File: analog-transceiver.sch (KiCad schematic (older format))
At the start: 142 parts, among them J1 BNC, J2 AF In, J3 AF Out, Q1 2N3904, Q10 2N3904, Q11 2N3904, Q12 2N3904, Q13 2N3904, Q14 2N3904, Q15 2N3904, Q16 2N3904, Q17 2N3904, Q18 BF245A, Q19 2N3906, Q2 2N3904, Q20 2N3904, Q21 BF245A, Q25 BD139, Q26 BD140, Q3 BF245A, SW1 SW_DPDT_x2, SW2 SW_DPDT_x2, T1 2:8 Turns 43-material? iron p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, T2 iron powerder, Y1 10MHz, Y2 10MHz, Y3 10MHz, Y4 10MHz

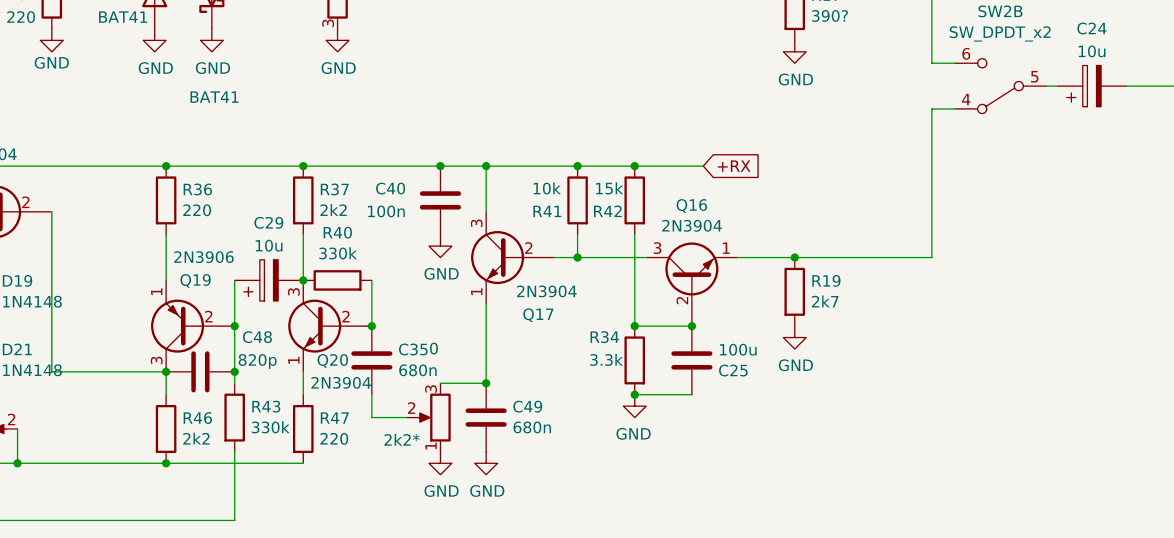
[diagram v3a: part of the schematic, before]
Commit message: Removed one stage from audio amplifier since the pre-amp should provide enough gain.
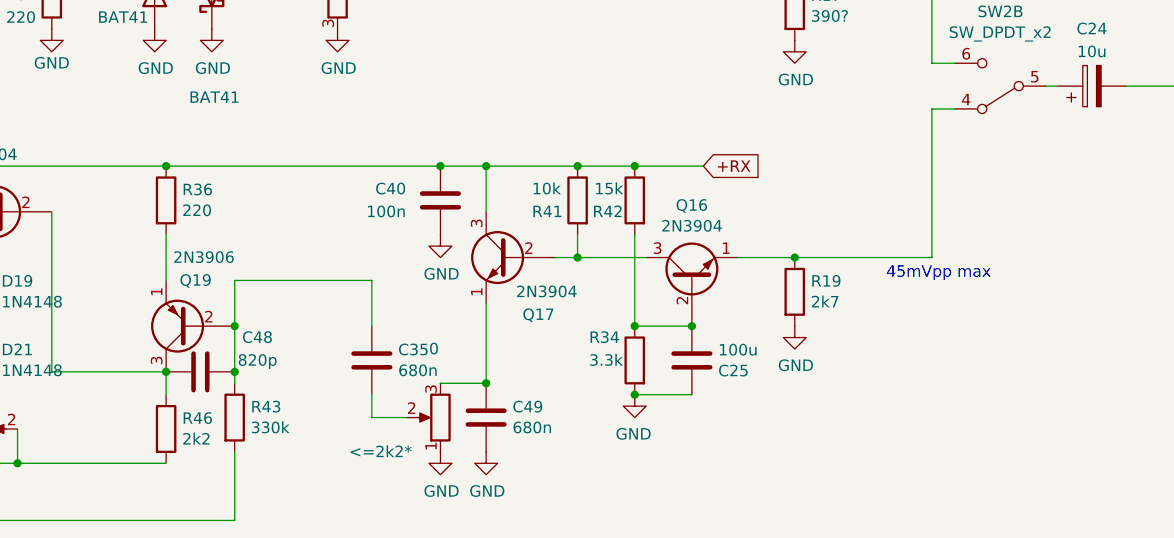
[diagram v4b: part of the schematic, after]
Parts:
- removed C29: 10u, Capacitor_THT:CP_Radial_D5.0mm_P2.50mm, symbol Device:CP
- removed Q20: 2N3904, Package_TO_SOT_THT:TO-92_Inline_Wide, symbol Transistor_BJT:2N3904
- removed R37: 2k2, Resistor_THT:R_Axial_DIN0207_L6.3mm_D2.5mm_P2.54mm_Vertical, symbol Device:R
- removed R40: 330k, Resistor_THT:R_Axial_DIN0207_L6.3mm_D2.5mm_P2.54mm_Vertical, symbol Device:R
- removed R47: 220, Resistor_THT:R_Axial_DIN0207_L6.3mm_D2.5mm_P2.54mm_Vertical, symbol Device:R
- renumbered 2k2* to <=2k2*
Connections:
- net at C35.2: now also C48.1, Q19.2 (B), R43.1
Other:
- note added: "45mVpp max"
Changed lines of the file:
@@
 	4550 9850 4250 9850
-$Comp
-L Transistor_BJT:2N3904 Q20
-U 1 1 5F8378DC
-P 3150 10150
-F 0 "Q20" H 3050 10000 50  0000 L CNN
-F 1 "2N3904" H 2950 9900 50  0000 L CNN
-F 2 "Package_TO_SOT_THT:TO-92_Inline_Wide" H 3350 10075 50  0001 L CIN
-F 3 "https://www.fairchildsemi.com/datasheets/2N/2N3904.pdf" H 3150 10150 50  0001 L CNN
-	1    3150 10150
-	-1   0    0    -1
-$EndComp
 $Comp
 L Transistor_BJT:2N3904 Q15
@@
 Wire Wire Line
 	2450 10450 2450 10350
-$Comp
-L Device:CP C29
-U 1 1 5F9EACF0
-P 2900 9950
-F 0 "C29" V 3150 9950 50  0000 C CNN
-F 1 "10u" V 3050 9950 50  0000 C CNN
-F 2 "Capacitor_THT:CP_Radial_D5.0mm_P2.50mm" H 2938 9800 50  0001 C CNN
-F 3 "~" H 2900 9950 50  0001 C CNN
-	1    2900 9950
-	0    -1   -1   0
-$EndComp
-$Comp
-L Device:R R37
-U 1 1 5FA27040
-P 3050 9600
-F 0 "R37" H 3120 9646 50  0000 L CNN
-F 1 "2k2" H 3120 9555 50  0000 L CNN
-F 2 "Resistor_THT:R_Axial_DIN0207_L6.3mm_D2.5mm_P2.54mm_Vertical" V 2980 9600 50  0001 C CNN
-F 3 "~" H 3050 9600 50  0001 C CNN
-	1    3050 9600
-	1    0    0    -1
-$EndComp
-$Comp
-L Device:R R47
-U 1 1 5FA27B26
-P 3050 10600
-F 0 "R47" H 3120 10646 50  0000 L CNN
-F 1 "220" H 3120 10555 50  0000 L CNN
-F 2 "Resistor_THT:R_Axial_DIN0207_L6.3mm_D2.5mm_P2.54mm_Vertical" V 2980 10600 50  0001 C CNN
-F 3 "~" H 3050 10600 50  0001 C CNN
-	1    3050 10600
-	1    0    0    -1
-$EndComp
-Wire Wire Line
-	2450 9450 3050 9450
-Wire Wire Line
-	3050 9750 3050 9950
-Connection ~ 3050 9950
 Wire Wire Line
 	2750 9950 2750 10150
-Wire Wire Line
-	3050 10350 3050 10450
 Connection ~ 2450 10350
 $Comp
@@
 Wire Wire Line
 	1150 10650 1150 10750
-Wire Wire Line
-	2450 10750 3050 10750
-Connection ~ 2450 10750
 $Comp
 L power:GND #PWR039
@@
 $EndComp
 Connection ~ 1150 10750
-$Comp
-L Device:R R40
-U 1 1 5FACC40B
-P 3200 9950
-F 0 "R40" V 3407 9950 50  0000 C CNN
-F 1 "330k" V 3316 9950 50  0000 C CNN
-F 2 "Resistor_THT:R_Axial_DIN0207_L6.3mm_D2.5mm_P2.54mm_Vertical" V 3130 9950 50  0001 C CNN
-F 3 "~" H 3200 9950 50  0001 C CNN
-	1    3200 9950
-	0    -1   -1   0
-$EndComp
 $Comp
 L Device:R R43
@@
 $EndComp
 $Comp
-L Device:R_POT 2k2*
+L Device:R_POT <=2k2*
 U 1 1 5FB97227
 P 3650 10550
-F 0 "2k2*" H 3900 10650 50  0000 R CNN
+F 0 "<=2k2*" H 4050 10700 50  0000 R CNN
 F 1 "0" H 3700 10250 50  0000 R CNN
 F 2 "Potentiometer_THT:Potentiometer_Vishay_T73XW_Horizontal" H 3650 10550 50  0001 C CNN
@@
 	1    0    0    -1
 $EndComp
-Connection ~ 3350 10150
 Wire Wire Line
 	3350 10450 3350 10550
@@
 Wire Wire Line
 	3650 10400 3850 10400
-Wire Wire Line
-	3050 9450 3650 9450
-Connection ~ 3050 9450
 Connection ~ 3850 9450
 Connection ~ 3650 9450
@@
 	5800 9200 5800 9850
 Connection ~ 5200 9850
+Wire Wire Line
+	2450 9450 3650 9450
+Wire Wire Line
+	2750 9950 3350 9950
+Text Notes 5600 9950 0    50   ~ 0
+45mVpp max
 $EndSCHEMATC

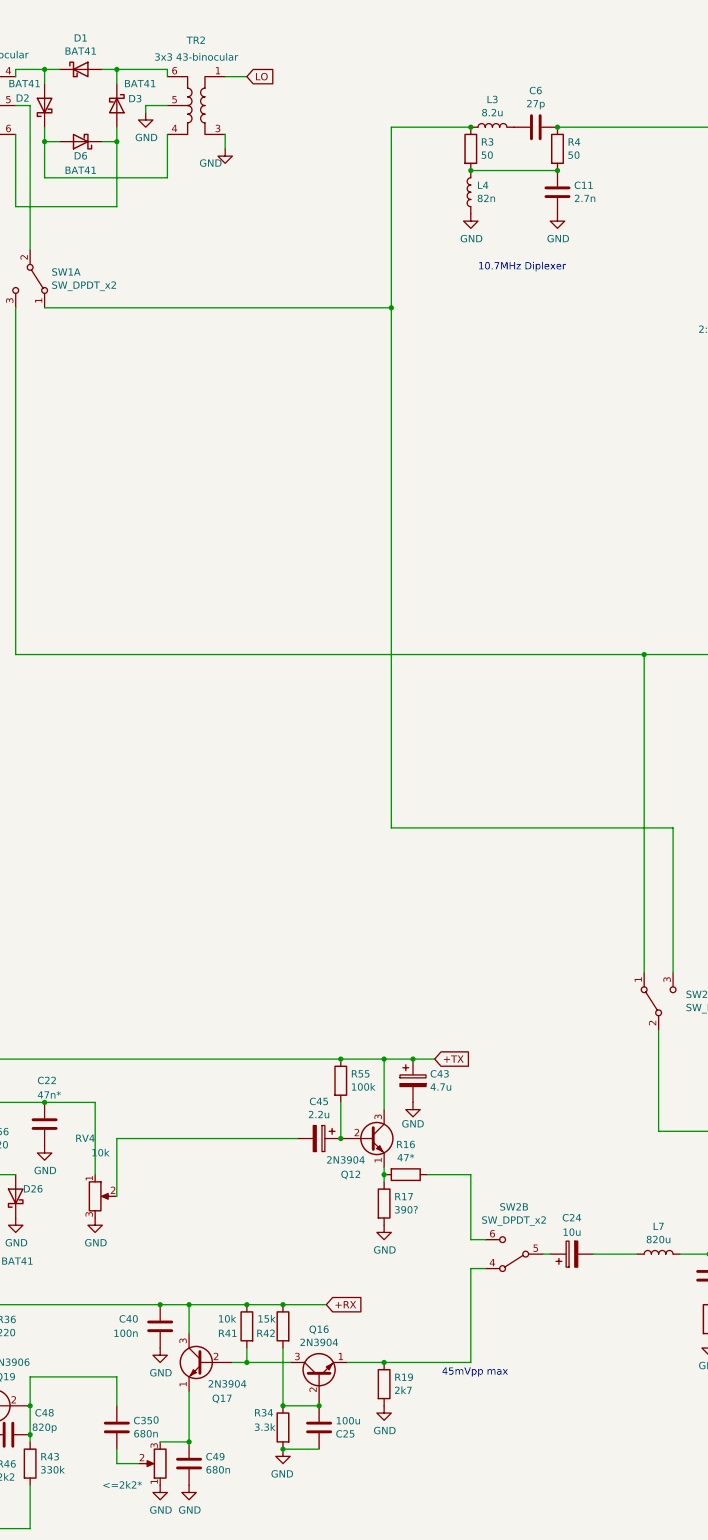
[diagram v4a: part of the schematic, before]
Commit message: Reworked diplexer values for smooth transition at 10.7MHz.
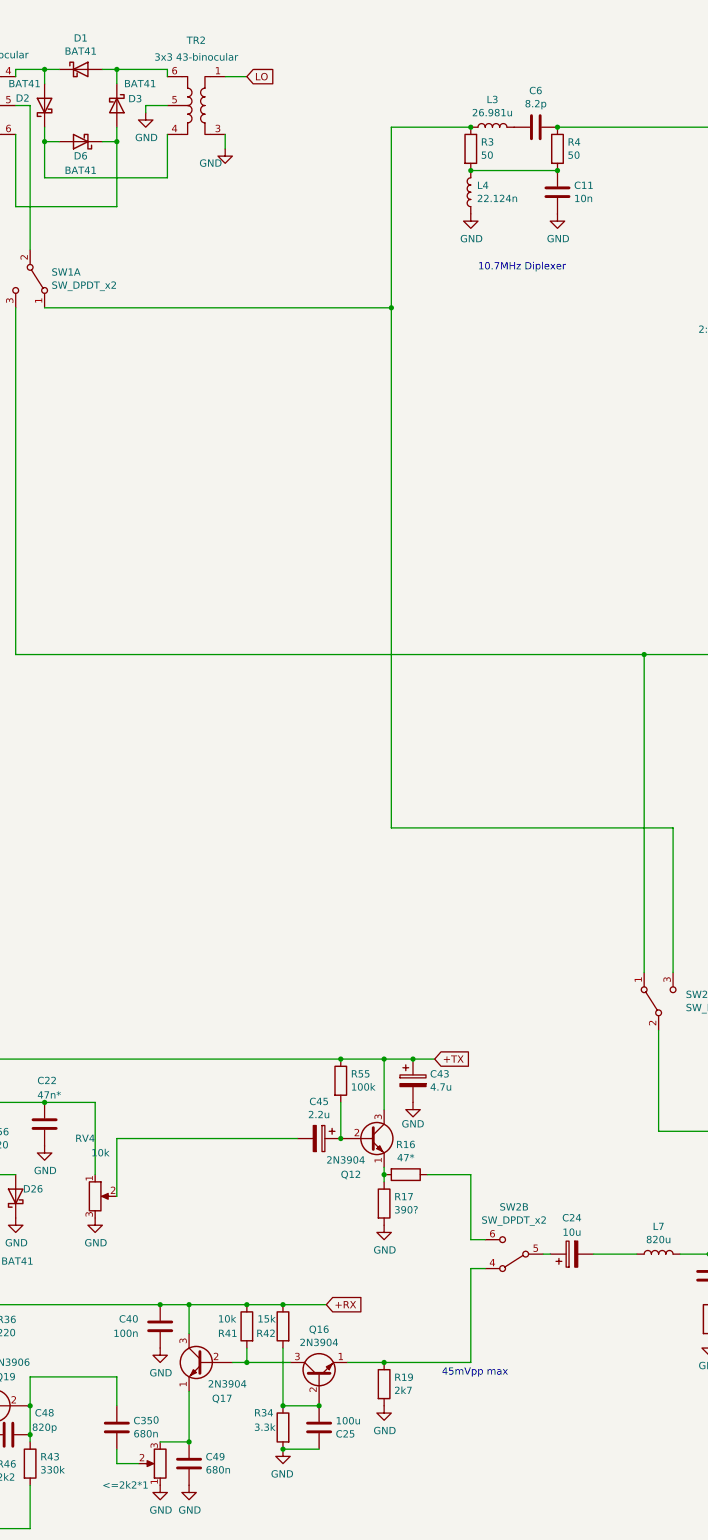
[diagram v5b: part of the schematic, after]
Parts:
- C11: value 2.7n -> 10n
- C6: value 27p -> 8.2p
- L3: value 8.2u -> 26.981u
- L4: value 82n -> 22.124n
- renumbered <=2k2* to <=2k2*1
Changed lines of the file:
@@
 $EndComp
 $Comp
-L Device:R_POT <=2k2*
+L Device:R_POT <=2k2*1
 U 1 1 5FB97227
 P 3650 10550
-F 0 "<=2k2*" H 4050 10700 50  0000 R CNN
+F 0 "<=2k2*1" H 4050 10700 50  0000 R CNN
 F 1 "0" H 3700 10250 50  0000 R CNN
 F 2 "Potentiometer_THT:Potentiometer_Vishay_T73XW_Horizontal" H 3650 10550 50  0001 C CNN
@@
 P 5950 1300
 F 0 "L3" V 6140 1300 50  0000 C CNN
-F 1 "8.2u" V 6049 1300 50  0000 C CNN
+F 1 "26.981u" V 6049 1300 50  0000 C CNN
 F 2 "Inductor_THT:L_Toroid_Vertical_L10.0mm_W5.0mm_P5.08mm" H 5950 1300 50  0001 C CNN
 F 3 "~" H 5950 1300 50  0001 C CNN
@@
 P 6250 1300
 F 0 "C6" V 5998 1300 50  0000 C CNN
-F 1 "27p" V 6089 1300 50  0000 C CNN
+F 1 "8.2p" V 6089 1300 50  0000 C CNN
 F 2 "Potentiometer_THT:Potentiometer_Piher_PT-6-V_Vertical" H 6288 1150 50  0001 C CNN
 F 3 "~" H 6250 1300 50  0001 C CNN
@@
 P 5800 1750
 F 0 "L4" H 5757 1704 50  0000 R CNN
-F 1 "82n" H 5757 1795 50  0000 R CNN
+F 1 "22.124n" H 5757 1795 50  0000 R CNN
 F 2 "Inductor_THT:L_Toroid_Vertical_L10.0mm_W5.0mm_P5.08mm" H 5800 1750 50  0001 C CNN
 F 3 "~" H 5800 1750 50  0001 C CNN
@@
 P 6400 1750
 F 0 "C11" H 6515 1796 50  0000 L CNN
-F 1 "2.7n" H 6515 1705 50  0000 L CNN
+F 1 "10n" H 6515 1705 50  0000 L CNN
 F 2 "Capacitor_THT:C_Disc_D3.8mm_W2.6mm_P2.50mm" H 6438 1600 50  0001 C CNN
 F 3 "~" H 6400 1750 50  0001 C CNN

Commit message: Added missing footprints for new components.
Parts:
- C17, C19, C33, C39: footprint (none) -> Capacitor_THT:C_Disc_D3.8mm_W2.6mm_P2.50mm
- J1: footprint Connector_Coaxial:BNC_Amphenol_B6252HB-NPP3G-50_Horizontal -> Connector_PinHeader_2.54mm:PinHeader_1x02_P2.54mm_Vertical
- L6, L7: footprint (none) -> Inductor_THT:L_Toroid_Vertical_L10.0mm_W5.0mm_P5.08mm
- R12: footprint (none) -> Resistor_THT:R_Axial_DIN0204_L3.6mm_D1.6mm_P5.08mm_Horizontal
- T1, T2: footprint (none) -> Button_Switch_THT:SW_NKK_G1xJP
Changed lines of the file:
@@
 F 0 "J1" H 1700 1200 50  0000 C CNN
 F 1 "BNC" H 1700 1100 50  0000 C CNN
-F 2 "Connector_Coaxial:BNC_Amphenol_B6252HB-NPP3G-50_Horizontal" H 1700 950 50  0001 C CNN
+F 2 "Connector_PinHeader_2.54mm:PinHeader_1x02_P2.54mm_Vertical" H 1700 950 50  0001 C CNN
 F 3 " ~" H 1700 950 50  0001 C CNN
 	1    1700 950
@@
 F 0 "T1" H 8000 1800 50  0000 C CNN
 F 1 "2:8 Turns 43-material? iron powder?" H 8000 1700 50  0000 C CNN
-F 2 "" H 8000 2200 50  0001 C CNN
+F 2 "Button_Switch_THT:SW_NKK_G1xJP" H 8000 2200 50  0001 C CNN
 F 3 "~" H 8000 2200 50  0001 C CNN
 	1    8000 2200
@@
 F 0 "L6" V 11640 1650 50  0000 C CNN
 F 1 "500n*" V 11549 1650 50  0000 C CNN
-F 2 "" H 11450 1650 50  0001 C CNN
+F 2 "Inductor_THT:L_Toroid_Vertical_L10.0mm_W5.0mm_P5.08mm" H 11450 1650 50  0001 C CNN
 F 3 "~" H 11450 1650 50  0001 C CNN
 	1    11450 1650
@@
 F 0 "C17" H 11050 1850 50  0000 L CNN
 F 1 "2n*" H 11050 1750 50  0000 L CNN
-F 2 "" H 11338 1650 50  0001 C CNN
+F 2 "Capacitor_THT:C_Disc_D3.8mm_W2.6mm_P2.50mm" H 11338 1650 50  0001 C CNN
 F 3 "~" H 11300 1800 50  0001 C CNN
 	1    11300 1800
@@
 F 0 "C19" H 11715 1846 50  0000 L CNN
 F 1 "500p*" H 11715 1755 50  0000 L CNN
-F 2 "" H 11638 1650 50  0001 C CNN
+F 2 "Capacitor_THT:C_Disc_D3.8mm_W2.6mm_P2.50mm" H 11638 1650 50  0001 C CNN
 F 3 "~" H 11600 1800 50  0001 C CNN
 	1    11600 1800
@@
 F 0 "T2" H 13550 5431 50  0000 C CNN
 F 1 "iron powerder" H 13550 5340 50  0000 C CNN
-F 2 "" H 13550 5050 50  0001 C CNN
+F 2 "Button_Switch_THT:SW_NKK_G1xJP" H 13550 5050 50  0001 C CNN
 F 3 "~" H 13550 5050 50  0001 C CNN
 	1    13550 5050
@@
 F 0 "C33" H 13265 5096 50  0000 L CNN
 F 1 "?" H 13265 5005 50  0000 L CNN
-F 2 "" H 13188 4900 50  0001 C CNN
+F 2 "Capacitor_THT:C_Disc_D3.8mm_W2.6mm_P2.50mm" H 13188 4900 50  0001 C CNN
 F 3 "~" H 13150 5050 50  0001 C CNN
 	1    13150 5050
@@
 F 0 "C39" H 7565 9296 50  0000 L CNN
 F 1 "330n" H 7565 9205 50  0000 L CNN
-F 2 "" H 7488 9100 50  0001 C CNN
+F 2 "Capacitor_THT:C_Disc_D3.8mm_W2.6mm_P2.50mm" H 7488 9100 50  0001 C CNN
 F 3 "~" H 7450 9250 50  0001 C CNN
 	1    7450 9250
@@
 F 0 "R12" H 7520 9596 50  0000 L CNN
 F 1 "50" H 7520 9505 50  0000 L CNN
-F 2 "" V 7380 9550 50  0001 C CNN
+F 2 "Resistor_THT:R_Axial_DIN0204_L3.6mm_D1.6mm_P5.08mm_Horizontal" V 7380 9550 50  0001 C CNN
 F 3 "~" H 7450 9550 50  0001 C CNN
 	1    7450 9550
@@
 F 0 "L7" V 7290 9100 50  0000 C CNN
 F 1 "820u" V 7199 9100 50  0000 C CNN
-F 2 "" H 7100 9100 50  0001 C CNN
+F 2 "Inductor_THT:L_Toroid_Vertical_L10.0mm_W5.0mm_P5.08mm" H 7100 9100 50  0001 C CNN
 F 3 "~" H 7100 9100 50  0001 C CNN
 	1    7100 9100

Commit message: New design + Rellay PTT + 1st Prototype v1.
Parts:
- removed C24: 10u, Capacitor_THT:CP_Radial_D5.0mm_P2.50mm, symbol Device:CP
- removed C27: 470u, Capacitor_THT:CP_Radial_D10.0mm_P2.50mm, symbol Device:CP
- removed C30: 220u, Capacitor_THT:CP_Radial_D10.0mm_P2.50mm, symbol Device:CP
- removed C34: 1u, Capacitor_THT:CP_Radial_D5.0mm_P2.50mm, symbol Device:CP
- removed C35: 680n, Capacitor_THT:C_Disc_D3.8mm_W2.6mm_P2.50mm, symbol Device:C
- removed C40: 100n, Capacitor_THT:C_Disc_D3.8mm_W2.6mm_P2.50mm, symbol Device:C
- removed C48: 820p, Capacitor_THT:C_Disc_D3.8mm_W2.6mm_P2.50mm, symbol Device:C
- removed D19, D21: 1N4148, Diode_THT:D_DO-35_SOD27_P7.62mm_Horizontal, symbol Diode:1N4148
- removed D20, D22, D23, D24: BAT41, Diode_THT:D_DO-35_SOD27_P7.62mm_Horizontal, symbol Diode:BAT41
- removed Q15, Q16, Q17: 2N3904, Package_TO_SOT_THT:TO-92_Inline_Wide, symbol Transistor_BJT:2N3904
- removed Q19: 2N3906, Package_TO_SOT_THT:TO-92_Inline_Wide, symbol Transistor_BJT:2N3906
- removed Q25: BD139, Package_TO_SOT_THT:TO-126-3_Vertical, symbol Transistor_BJT:BD139
- removed Q26: BD140, Package_TO_SOT_THT:TO-126-3_Vertical, symbol Transistor_BJT:BD140
- removed R42: 15k, Resistor_THT:R_Axial_DIN0207_L6.3mm_D2.5mm_P2.54mm_Vertical, symbol Device:R
- removed R43: 330k, Resistor_THT:R_Axial_DIN0207_L6.3mm_D2.5mm_P2.54mm_Vertical, symbol Device:R
- removed R46: 2k2, Resistor_THT:R_Axial_DIN0207_L6.3mm_D2.5mm_P2.54mm_Vertical, symbol Device:R
- removed SW1, SW2: SW_DPDT_x2, Button_Switch_THT:SW_NKK_G1xJP, symbol Switch:SW_DPDT_x2
- removed TR6: 3x3 43-toroid, Button_Switch_THT:SW_NKK_G1xJP, symbol analog-transceiver-rescue:ADT1-1WT-Transformer
- added C24, C27, C30, C56: 100n, Capacitor_THT:C_Disc_D3.8mm_W2.6mm_P2.50mm, symbol Device:C
- added C29, C34: 5p6, Capacitor_THT:C_Disc_D3.8mm_W2.6mm_P2.50mm, symbol Device:C
- added C35: 470u, Capacitor_THT:CP_Radial_D10.0mm_P2.50mm, symbol Device:CP
- added C40: CTRIM, Potentiometer_THT:Potentiometer_Piher_PT-6-V_Vertical, symbol Device:CTRIM
- added C41: 10u, Capacitor_THT:CP_Radial_D5.0mm_P2.50mm, symbol Device:CP
- added C42: 330n, Capacitor_THT:C_Disc_D3.8mm_W2.6mm_P2.50mm, symbol Device:C
- added C46: 220u, Capacitor_THT:CP_Radial_D10.0mm_P2.50mm, symbol Device:CP
- added C47: 1u, Capacitor_THT:CP_Radial_D5.0mm_P2.50mm, symbol Device:CP
- added C48, C54: CP, Capacitor_THT:CP_Radial_D5.0mm_P2.50mm, symbol Device:CP
- added C50: 100u, Capacitor_THT:CP_Radial_D5.0mm_P2.50mm, symbol Device:C
- added C51: 820p needed?, Capacitor_THT:C_Disc_D3.8mm_W2.6mm_P2.50mm, symbol Device:C
- added C52, C55: C, Capacitor_THT:C_Disc_D3.8mm_W2.6mm_P2.50mm, symbol Device:C
- added C53: 680n, Capacitor_THT:C_Disc_D3.8mm_W2.6mm_P2.50mm, symbol Device:C
- added D10, D5, D7, D9: BAT41, Diode_THT:D_DO-35_SOD27_P7.62mm_Horizontal, symbol Diode:BAT41
- added D11, D12: 1n4007, Diode_THT:D_A-405_P7.62mm_Horizontal, symbol Device:D
- added D4, D8: 1N4148, Diode_THT:D_DO-35_SOD27_P2.54mm_Vertical_AnodeUp, symbol Diode:1N4148
- added K1, K2: G5Q-1, Relay_THT:Relay_SPDT_Omron-G5Q-1, symbol Relay:G5Q-1
- added Q15: 2N3906, Package_TO_SOT_THT:TO-92_Inline_Wide, symbol Transistor_BJT:2N3906
- added Q16: BD140, Package_TO_SOT_THT:TO-126-3_Vertical, symbol Transistor_BJT:BD140
- added Q17: 2n3904, Package_TO_SOT_THT:TO-92_Inline_Wide, symbol Device:Q_NPN_EBC
- added Q19: 2n2904, Package_TO_SOT_THT:TO-92_Inline_Wide, symbol Device:Q_NPN_EBC
- added Q4, Q5, Q6, Q8, Q9: 2N3904, Package_TO_SOT_THT:TO-92_Inline_Wide, symbol Transistor_BJT:2N3904
- added Q7: BD139, Package_TO_SOT_THT:TO-126-3_Vertical, symbol Transistor_BJT:BD139
- added R13: N/A, Resistor_THT:R_Axial_DIN0204_L3.6mm_D1.6mm_P5.08mm_Horizontal, symbol Device:R
- added R18: 39, Resistor_THT:R_Axial_DIN0204_L3.6mm_D1.6mm_P5.08mm_Horizontal, symbol Device:R
- added R20: 220, Resistor_THT:R_Axial_DIN0207_L6.3mm_D2.5mm_P2.54mm_Vertical, symbol Device:R
- added R21: 10k, Resistor_THT:R_Axial_DIN0207_L6.3mm_D2.5mm_P2.54mm_Vertical, symbol Device:R
- added R22: 15k, Resistor_THT:R_Axial_DIN0207_L6.3mm_D2.5mm_P2.54mm_Vertical, symbol Device:R
- added R29: 470, Resistor_THT:R_Axial_DIN0207_L6.3mm_D2.5mm_P2.54mm_Vertical, symbol Device:R
- added R30: 2k7, Resistor_THT:R_Axial_DIN0207_L6.3mm_D2.5mm_P2.54mm_Vertical, symbol Device:R
- added R32: 3.3k, Resistor_THT:R_Axial_DIN0207_L6.3mm_D2.5mm_P2.54mm_Vertical, symbol Device:R
- added R33: 50, Resistor_THT:R_Axial_DIN0204_L3.6mm_D1.6mm_P5.08mm_Horizontal, symbol Device:R
- added R35, R40: 4k7, Resistor_THT:R_Axial_DIN0207_L6.3mm_D2.5mm_P2.54mm_Vertical, symbol Device:R
- added R37: 2k2, Resistor_THT:R_Axial_DIN0207_L6.3mm_D2.5mm_P2.54mm_Vertical, symbol Device:R
- added RV2: 5k, Potentiometer_THT:Potentiometer_Piher_PT-6-V_Vertical, symbol Device:R_POT
- added TR3: 3x3 43-binocular, Button_Switch_THT:SW_NKK_G1xJP, symbol analog-transceiver-rescue:ADT1-1WT-Transformer
- added TR4: 3x3 43-toroid, Button_Switch_THT:SW_NKK_G1xJP, symbol analog-transceiver-rescue:ADT1-1WT-Transformer
- C25: value 100u -> 5p6
- C39: value 330n -> 100n
- C6: footprint Potentiometer_THT:Potentiometer_Piher_PT-6-V_Vertical -> Capacitor_THT:C_Disc_D3.8mm_W2.6mm_P2.50mm
- R12: value 50 -> 180k
- R14: value <10R* -> 1k
- R15: value <15R* -> 180k
- R16: value 47* -> N/A
- R17: value 390? -> 1k
- R19: value 2k7 -> 1k
- R23: value 100K -> 180k
- R34: value 3.3k -> 4k7
- R36: value 220 -> 330k
- R38: value 47 -> 39
- R39: value 390 -> 1k
- R41: value 10k -> 4k7; footprint Resistor_THT:R_Axial_DIN0204_L3.6mm_D1.6mm_P5.08mm_Horizontal -> Resistor_THT:R_Axial_DIN0207_L6.3mm_D2.5mm_P2.54mm_Vertical
- R55: value 100k -> 180k
- RV3: value 100R -> 100
- RV5: value 5k -> 4k7
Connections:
- net +12V: no longer C2.1, L5.1, R1.1
- net +RX: now also C2.1, C39.1, L5.1, R1.1, R15.1, C27.1, C35.1, Q5.3 (C), Q6.3 (C), Q7.2 (C), Q8.3 (C), R20.1, R21.1, R22.1; no longer R36.1, R41.1
- net +TX: now also R12.1, R34.2, C24.1, D11.1 (K), D12.1 (K), K1.1, K2.5, Q4.3 (C), R29.1, R35.2
- net BFO: now also K2.2
- net GND: now also C39.2, R14.2, R16.2, R41.2, TR5.3, TR5.5, C24.2, C27.2, C35.2, C40.1, C50.2, C52.2, C53.2, C54.2, C55.2, D11.2 (A), D12.2 (A), K1.5, K2.1, Q16.2 (C), R13.2, R30.2, R32.2, R33.2, R37.2, R40.2, RV2.2, RV2.3, TR3.1, TR4.1; no longer C25.2, C49.2, R12.2, R34.2, RV5.2, TR5.1
- net at TR1.5: now also L3.1, R3.1
- net at TR5.4: now also D10.2 (A), D9.1 (K); no longer R14.2
- net at R14.1: now also R38.2, Q4.1 (E)
- net at RV3.1: now also Q19.1 (E); no longer R15.1
- net at L7.1: now also C41.2
- net at Q12.1 (E), R17.1: now also C48.1; no longer R16.2
- net at R34.1: now also C54.1, C55.1, Q17.2 (B), R40.1; no longer C25.1
- net at <=2k2*1.3: now also C53.1, Q8.1 (E); no longer C49.1
- net at R19.1: now also Q5.1 (E), R18.2
- net at RV5.1: now also RV3.2
- net at R36.2: now also C46.1, Q16.1 (E), Q7.1 (E)
- net at J3.2 (Pin_2): now also C46.2
- net at <=2k2*1.2: now also C49.1
- net at Q10.1 (E), R39.1: now also C25.2, C29.2; no longer R38.2
- net at C36.2: now also K1.3
- net at R16.1: now also R15.2, C29.1, Q5.2 (B)
- net at C6.1, R4.1: now also K1.2; no longer T1.1 (AA)
- net at C13.1, Q1.2 (B), R2.2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: now also C34.1
- new net: K1.4, T1.1 (AA)
- new net: C56.1, K2.3
- new net: K2.4, TR5.1
- new net: Q17.1 (E), RV3.3
- new net: Q17.3 (C), TR3.6
- new net: C48.2, Q19.2 (B), R35.1, R41.1
- new net: Q19.3 (C), TR3.4
- new net: C34.2, C40.2, TR3.3
- new net: C52.1, R29.2, TR3.5
- new net: C47.2, D8.1 (K), Q16.3 (B), RV2.1
- new net: C47.1, D4.2 (A), Q6.1 (E), Q7.3 (B)
- new net: C49.2, C51.1, Q15.2 (B), R36.1
- new net: C51.2, Q15.3 (C), Q6.2 (B), R37.1
- new net: Q15.1 (E), R20.2
- new net: D4.1 (K), D8.2 (A)
- new net: C41.1, Q9.1 (E), R30.1
- new net: C50.1, Q9.2 (B), R22.2, R32.1
- new net: Q8.2 (B), Q9.3 (C), R21.2
- new net: C42.1, L7.2, TR4.5
- new net: C42.2, R33.1
- new net: D5.2 (A), D7.1 (K), TR5.6
- new net: D5.1 (K), D9.2 (A), TR4.6
- new net: D10.1 (K), D7.2 (A), TR4.4
- new net: C30.1, TR4.3
- new net: C25.1, Q4.2 (B), R12.2, R13.1
- new net: C30.2, R18.1
- new net: C56.2, RV5.2
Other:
- note added: "45mVp max"
- note added: "Z-match here?"
- note added: "is 10u sufficient for 50ohm on <50Hz??"
- note removed: "45mVpp max"
- moved on the sheet: C1, C10, C11, C12, C13, C14, C15, C16, C17, C18, C19, C2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
